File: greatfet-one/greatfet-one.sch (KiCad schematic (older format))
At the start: 103 parts, among them J1 NEIGHBOR1, J2 NEIGHBOR2, J3 USB-MICRO-B-SHIELDED, J4 USB-MICRO-B-SHIELDED, J5 JTAG, J6 POWER, J7 BONUS_ROW, SW1 DFU, SW2 RESET, U1 LPC4330FBD144, U2 W25Q16DV, U3 AP7333, U4 IP4220CZ6, U5 AP2553W6-7, X1 MCU_XTAL, X2 RTC_XTAL

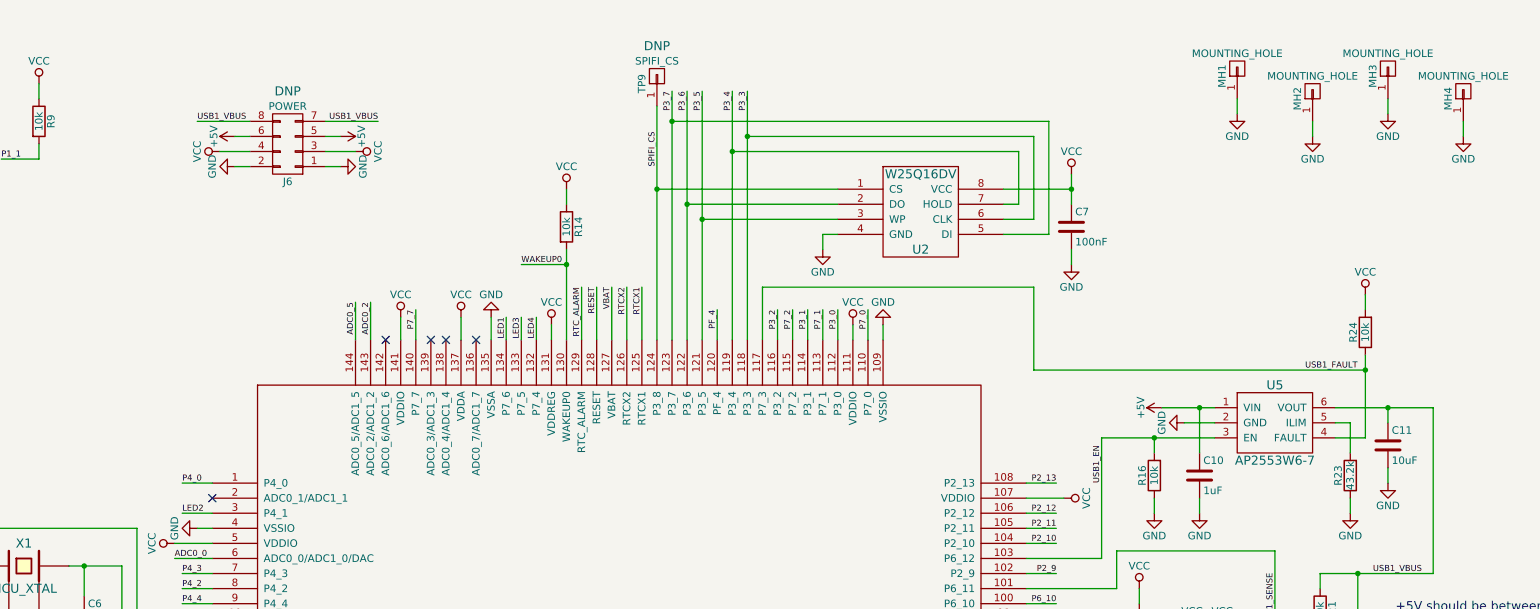
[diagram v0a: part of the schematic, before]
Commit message: GreatFET One: added ADC pin straps for hardware version detection
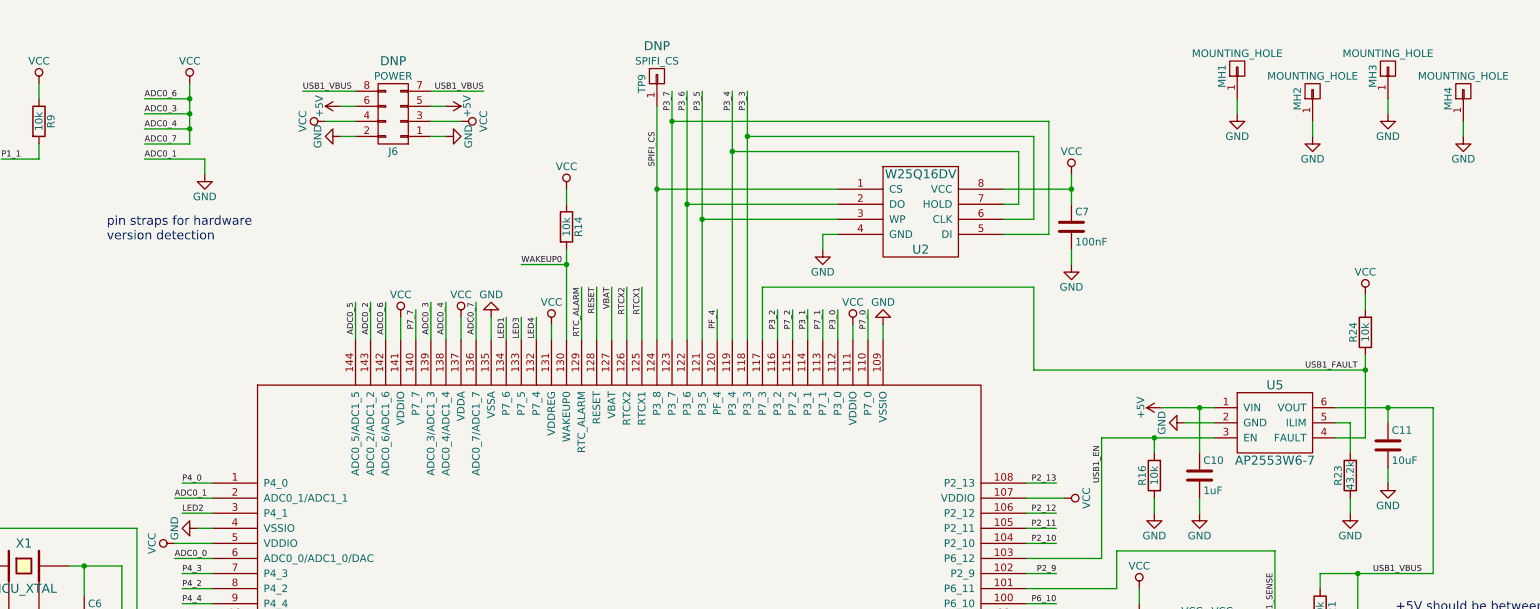
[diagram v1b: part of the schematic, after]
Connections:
- net GND: now also U1.2 (ADC0_1/ADC1_1)
- net VCC: now also U1.136 (ADC0_7/ADC1_7), U1.138 (ADC0_4/ADC1_4), U1.139 (ADC0_3/ADC1_3), U1.142 (ADC0_6/ADC1_6)
- no-connect marks 7 -> 2
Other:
- note added: "pin straps for hardware\nversion detection"
- moved on the sheet: J6
